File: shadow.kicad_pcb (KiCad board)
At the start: 2 copper layers, 69.8 x 78.7 mm, 95 parts, among them IC2 XB8089D, J1 USB_C_Receptacle, SW1 SW_Push, SW2 SW_Push, SW3 SW_SPST, U1 TCA9548APWR, U2 TCA9548APWR, U3 BQ24092DGQR, U4 TPS61085DGKR, U5 TPS259621DDAT

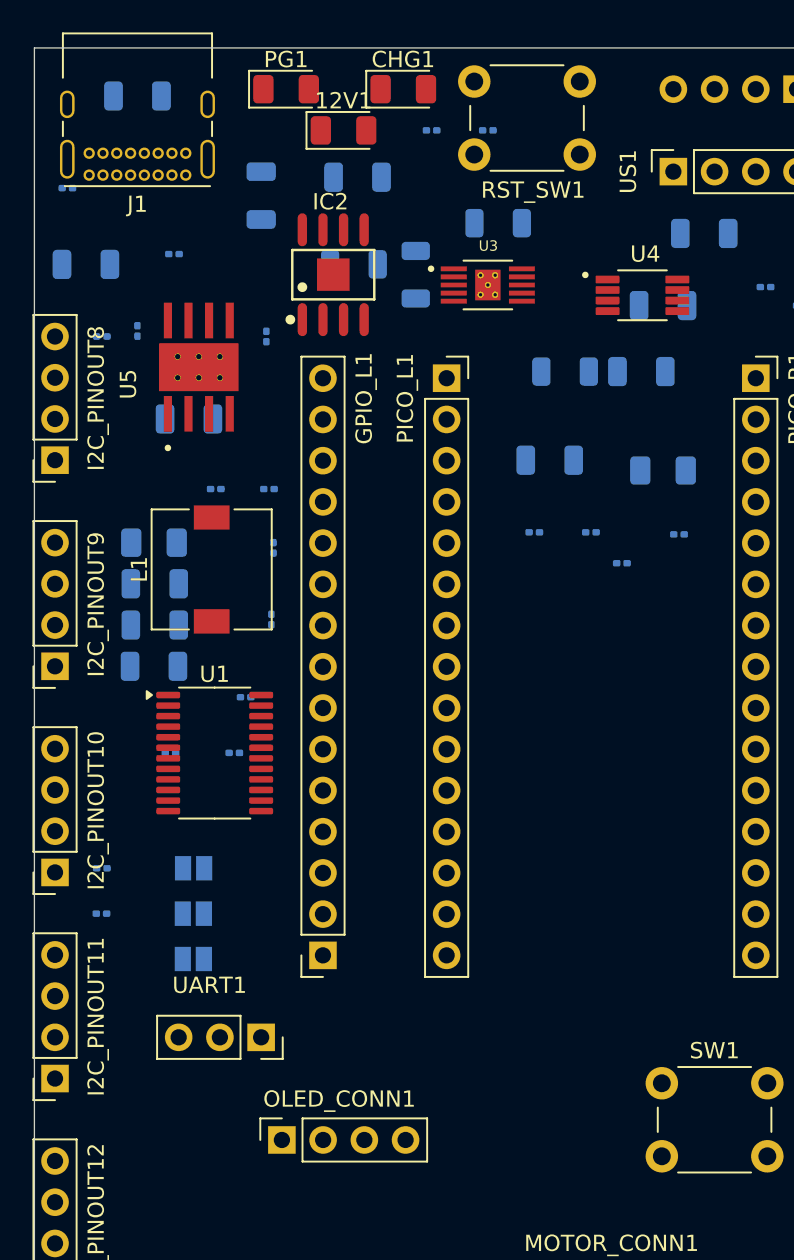
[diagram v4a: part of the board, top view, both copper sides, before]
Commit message: make pcb smaller
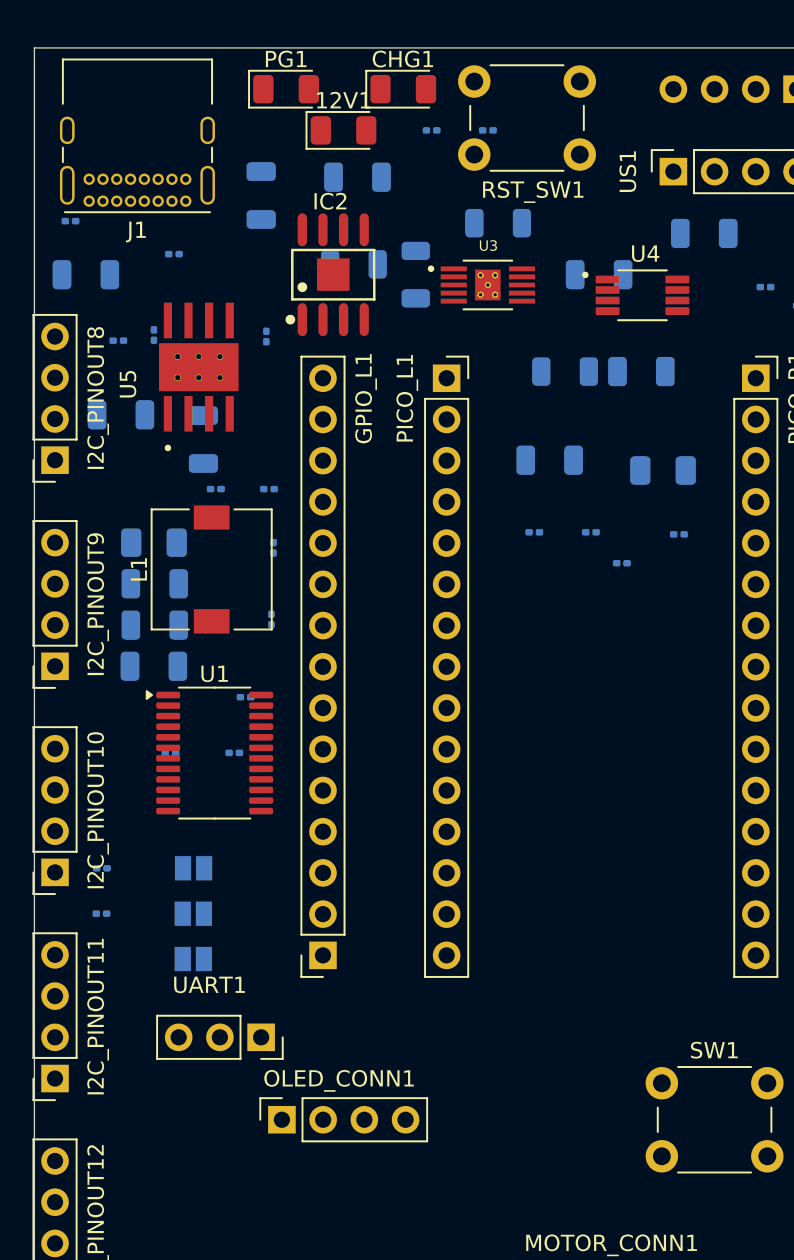
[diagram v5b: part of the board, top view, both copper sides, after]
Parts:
- moved C3 21.6 mm to (95.5, 90.2), turned to -90 degrees
- moved C2 4.37 mm to (119.9, 80.0)
- moved C10 4.20 mm to (90.4, 88.6)
- moved R30 2.04 mm to (87.3, 76.7)
- moved J1 1.61 mm to (94.4, 75.5)
- moved OLED_CONN1 1.24 mm to (100.3, 132.1)
- moved R12 1.05 mm to (92.5, 83.7)
- moved R13 1.05 mm to (90.3, 84.1)
- moved C7 0.64 mm to (88.3, 80.0)
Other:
- board text removed: "OLED TODO: move"
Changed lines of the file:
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@@
 		(tags "connector JST XH vertical")
 		(property "Reference" "BATT_JST1"
-			(at 0.976 4.572 360)
+			(at 0.976 4.572 0)
 			(layer "F.SilkS")
 			(effects
@@
 		)
 		(property "Value" "JST"
-			(at 1.25 4.6 360)
+			(at 1.25 4.6 0)
 			(layer "F.Fab")
 			(effects
@@
 		)
 		(fp_text user "${REFERENCE}"
-			(at 1.25 2.7 360)
+			(at 1.25 2.7 0)
 			(layer "F.Fab")
 			(effects
@@
 		(tags "Through hole socket strip THT 1x03 2.54mm single row")
 		(property "Reference" "UART1"
-			(at -3.2 3.175 360)
+			(at -3.2 3.175 0)
 			(layer "F.SilkS")
 			(effects
@@
 		)
 		(fp_text user "${REFERENCE}"
-			(at 0 2.54 360)
+			(at 0 2.54 0)
 			(layer "F.Fab")
 			(effects
@@
 	(footprint "Connector_PinSocket_2.54mm:PinSocket_1x04_P2.54mm_Vertical"
 		(layer "F.Cu")
-		(at 100.34 133.325 90)
+		(at 100.34 132.08 90)
 		(descr "Through hole straight socket strip, 1x04, 2.54mm pitch, single row (from Kicad 4.0.7), script generated")
 		(tags "Through hole socket strip THT 1x04 2.54mm single row")
@@
 		)
 		(property "Value" "Conn_01x04"
-			(at 0 10.16 90)
+			(at -0.025 3.8 180)
 			(layer "F.Fab")
 			(effects
@@
 		)
 		(fp_text user "${REFERENCE}"
-			(at 0 -2.54 90)
+			(at -3.835 3.8 0)
 			(layer "F.Fab")
 			(effects
@@
 	(footprint "Connector_USB:USB_C_Receptacle_GCT_USB4085"
 		(layer "F.Cu")
-		(at 94.415 73.875 180)
+		(at 94.415 75.48 180)
 		(descr "USB 2.0 Type C Receptacle, https://gct.co/Files/Drawings/USB4085.pdf")
 		(tags "USB Type-C Receptacle Through-hole Right angle")
@@
 		(placed yes)
 		(layer "B.Cu")
-		(at 89.245 83.82 180)
+		(at 90.261 84.074 180)
 		(descr "Resistor SMD 0201 (0603 Metric), square (rectangular) end terminal, IPC_7351 nominal, (Body size source: https://www.vishay.com/docs/20052/crcw0201e3.pdf), generated with kicad-footprint-generator")
 		(tags "resistor")
@@
 		(placed yes)
 		(layer "B.Cu")
-		(at 88.265 79.375 180)
+		(at 88.265 80.01 180)
 		(descr "Capacitor SMD 1206 (3216 Metric), square (rectangular) end terminal, IPC_7351 nominal, (Body size source: IPC-SM-782 page 76, https://www.pcb-3d.com/wordpress/wp-content/uploads/ipc-sm-782a_amendment_1_and_2.pdf), generated with kicad-footprint-generator")
 		(tags "capacitor")
@@
 		(placed yes)
 		(layer "B.Cu")
-		(at 94.615 88.9 180)
+		(at 90.424 88.646 180)
 		(descr "Capacitor SMD 1206 (3216 Metric), square (rectangular) end terminal, IPC_7351 nominal, (Body size source: IPC-SM-782 page 76, https://www.pcb-3d.com/wordpress/wp-content/uploads/ipc-sm-782a_amendment_1_and_2.pdf), generated with kicad-footprint-generator")
 		(tags "capacitor")
@@
 		(placed yes)
 		(layer "B.Cu")
-		(at 123.825 81.915 180)
+		(at 119.888 80.01 180)
 		(descr "Capacitor SMD 1206 (3216 Metric), square (rectangular) end terminal, IPC_7351 nominal, (Body size source: IPC-SM-782 page 76, https://www.pcb-3d.com/wordpress/wp-content/uploads/ipc-sm-782a_amendment_1_and_2.pdf), generated with kicad-footprint-generator")
 		(tags "capacitor")
@@
 		(placed yes)
 		(layer "B.Cu")
-		(at 87.122 74.676)
+		(at 87.31 76.708)
 		(descr "Resistor SMD 0201 (0603 Metric), square (rectangular) end terminal, IPC_7351 nominal, (Body size source: https://www.vishay.com/docs/20052/crcw0201e3.pdf), generated with kicad-footprint-generator")
 		(tags "resistor")
 		(property "Reference" "R30"
-			(at 0 1.05 0)
+			(at 2.195 0 0)
 			(layer "B.SilkS")
 			(effects
@@
 		(tags "capacitor")
 		(property "Reference" "C6"
-			(at 0 1.85 0)
+			(at -0.1925 1.905 0)
 			(layer "B.SilkS")
 			(effects
@@
 		(placed yes)
 		(layer "B.Cu")
-		(at 91.44 69 180)
+		(at 95.504 90.17 -90)
 		(descr "Capacitor SMD 1206 (3216 Metric), square (rectangular) end terminal, IPC_7351 nominal, (Body size source: IPC-SM-782 page 76, https://www.pcb-3d.com/wordpress/wp-content/uploads/ipc-sm-782a_amendment_1_and_2.pdf), generated with kicad-footprint-generator")
 		(tags "capacitor")
 		(property "Reference" "C3"
-			(at 0 1.85 0)
+			(at 0 1.85 90)
 			(layer "B.SilkS")
 			(effects
@@
 		)
 		(property "Value" "10uF"
-			(at 0 -1.85 0)
+			(at 0 -1.85 90)
 			(layer "B.Fab")
 			(effects
@@
 		)
 		(property "Footprint" "Capacitor_SMD:C_1206_3216Metric"
-			(at 0 0 0)
+			(at 0 0 90)
 			(unlocked yes)
 			(layer "B.Fab")
@@
 		)
 		(property "Datasheet" ""
-			(at 0 0 0)
+			(at 0 0 90)
 			(unlocked yes)
 			(layer "B.Fab")
@@
 		)
 		(property "Description" "Unpolarized capacitor"
-			(at 0 0 0)
+			(at 0 0 90)
 			(unlocked yes)
 			(layer "B.Fab")
@@
 		)
 		(fp_line
-			(start 2.3 1.15)
-			(end -2.3 1.15)
+			(start -2.3 1.15)
+			(end -2.3 -1.15)
 			(stroke
 				(width 0.05)
@@
 		)
 		(fp_line
-			(start 2.3 -1.15)
-			(end 2.3 1.15)
+			(start 2.3 1.15)
+			(end -2.3 1.15)
 			(stroke
 				(width 0.05)
@@
 		)
 		(fp_line
-			(start -2.3 1.15)
-			(end -2.3 -1.15)
+			(start -2.3 -1.15)
+			(end 2.3 -1.15)
 			(stroke
 				(width 0.05)
@@
 		)
 		(fp_line
-			(start -2.3 -1.15)
-			(end 2.3 -1.15)
+			(start 2.3 -1.15)
+			(end 2.3 1.15)
 			(stroke
 				(width 0.05)
@@
 		)
 		(fp_line
-			(start 1.6 0.8)
-			(end -1.6 0.8)
+			(start -1.6 0.8)
+			(end -1.6 -0.8)
 			(stroke
 				(width 0.1)
@@
 		)
 		(fp_line
-			(start 1.6 -0.8)
-			(end 1.6 0.8)
+			(start 1.6 0.8)
+			(end -1.6 0.8)
 			(stroke
 				(width 0.1)
@@
 		)
 		(fp_line
-			(start -1.6 0.8)
-			(end -1.6 -0.8)
+			(start -1.6 -0.8)
+			(end 1.6 -0.8)
 			(stroke
 				(width 0.1)
@@
 		)
 		(fp_line
-			(start -1.6 -0.8)
-			(end 1.6 -0.8)
+			(start 1.6 -0.8)
+			(end 1.6 0.8)
 			(stroke
 				(width 0.1)
@@
 		)
 		(fp_text user "${REFERENCE}"
-			(at 0 0 0)
+			(at 0 0 90)
 			(layer "B.Fab")
 			(effects
@@
 		)
 		(pad "1" smd roundrect
-			(at -1.475 0 180)
+			(at -1.475 0 270)
 			(size 1.15 1.8)
 			(layers "B.Cu" "B.Paste" "B.Mask")
@@
 		)
 		(pad "2" smd roundrect
-			(at 1.475 0 180)
+			(at 1.475 0 270)
 			(size 1.15 1.8)
 			(layers "B.Cu" "B.Paste" "B.Mask")
@@
 		(placed yes)
 		(layer "B.Cu")
-		(at 91.44 83.475 90)
+		(at 92.456 83.729 90)
 		(descr "Resistor SMD 0201 (0603 Metric), square (rectangular) end terminal, IPC_7351 nominal, (Body size source: https://www.vishay.com/docs/20052/crcw0201e3.pdf), generated with kicad-footprint-generator")
 		(tags "resistor")
@@
 		)
 	)
-	(gr_text "OLED\nTODO: move"
-		(at 101.6 139.7 0)
-		(layer "User.2")
-		(effects
-			(font
-				(size 1 1)
-				(thickness 0.15)
-			)
-			(justify left bottom)
-		)
-	)

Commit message: more work on pcb
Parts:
- moved C14 0.38 mm to (98.1, 106.4)
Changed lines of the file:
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@@
 		)
 		(property "Value" "TCA9548APWR"
-			(at 24.155 3.27 0)
+			(at -1.2015 1.513 0)
 			(layer "B.Fab")
 			(effects
@@
 		(at 95.22 85.71 90)
 		(property "Reference" "U5"
-			(at -1.05 -4.335 90)
+			(at 4.938 -0.224 180)
 			(layer "F.SilkS")
 			(effects
@@
 		(tags "LED")
 		(property "Reference" "12V1"
-			(at 0 -1.82 0)
+			(at 0 2.032 0)
 			(layer "F.SilkS")
 			(effects
@@
 		(tags "resistor")
 		(property "Reference" "R33"
-			(at 0 1.05 90)
+			(at 2.123 -0.127 90)
 			(layer "B.SilkS")
 			(effects
@@
 		(placed yes)
 		(layer "B.Cu")
-		(at 98.105 106.045 180)
+		(at 98.105 106.426 180)
 		(descr "Capacitor SMD 0201 (0603 Metric), square (rectangular) end terminal, IPC_7351 nominal, (Body size source: https://www.vishay.com/docs/20052/crcw0201e3.pdf), generated with kicad-footprint-generator")
 		(tags "capacitor")
 		(property "Reference" "C14"
-			(at 0.091 -1.016 0)
+			(at 2.347 -0.127 0)
 			(layer "B.SilkS")
 			(effects

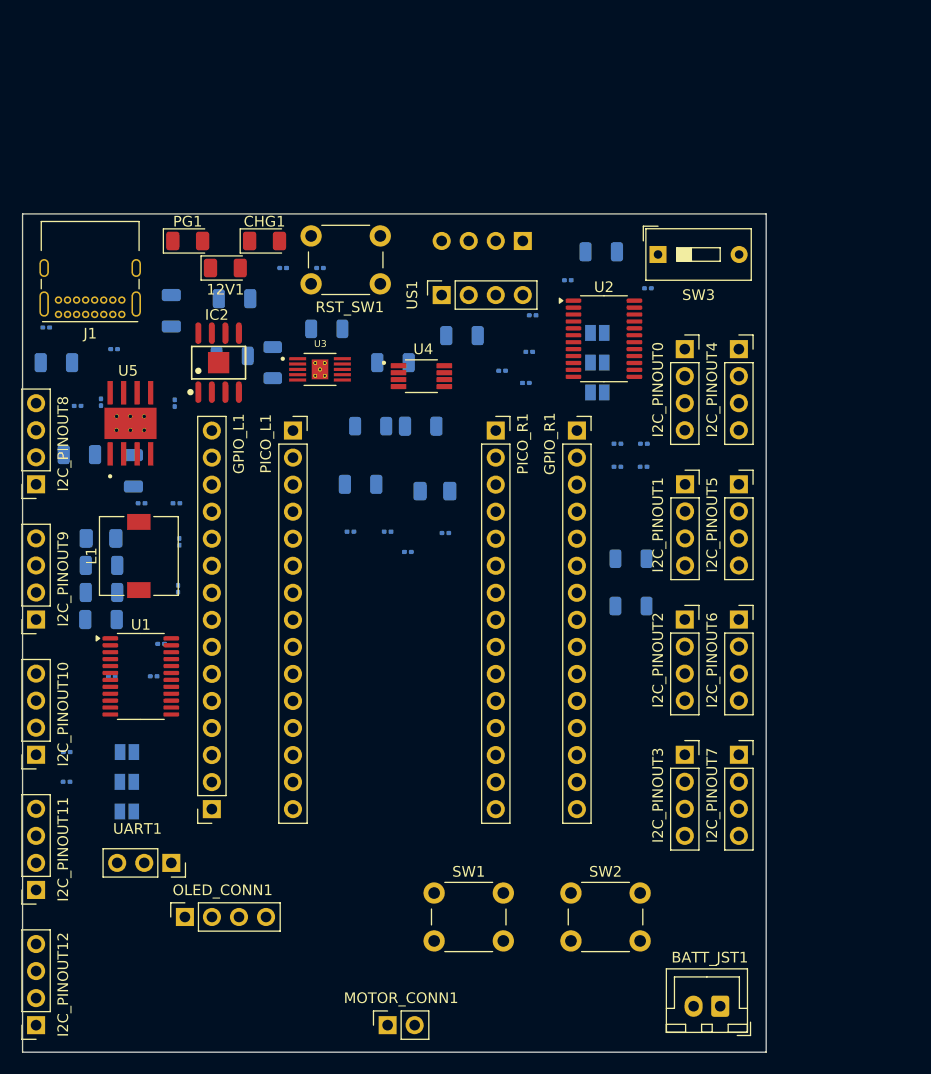
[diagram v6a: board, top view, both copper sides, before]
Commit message: add mounting holes
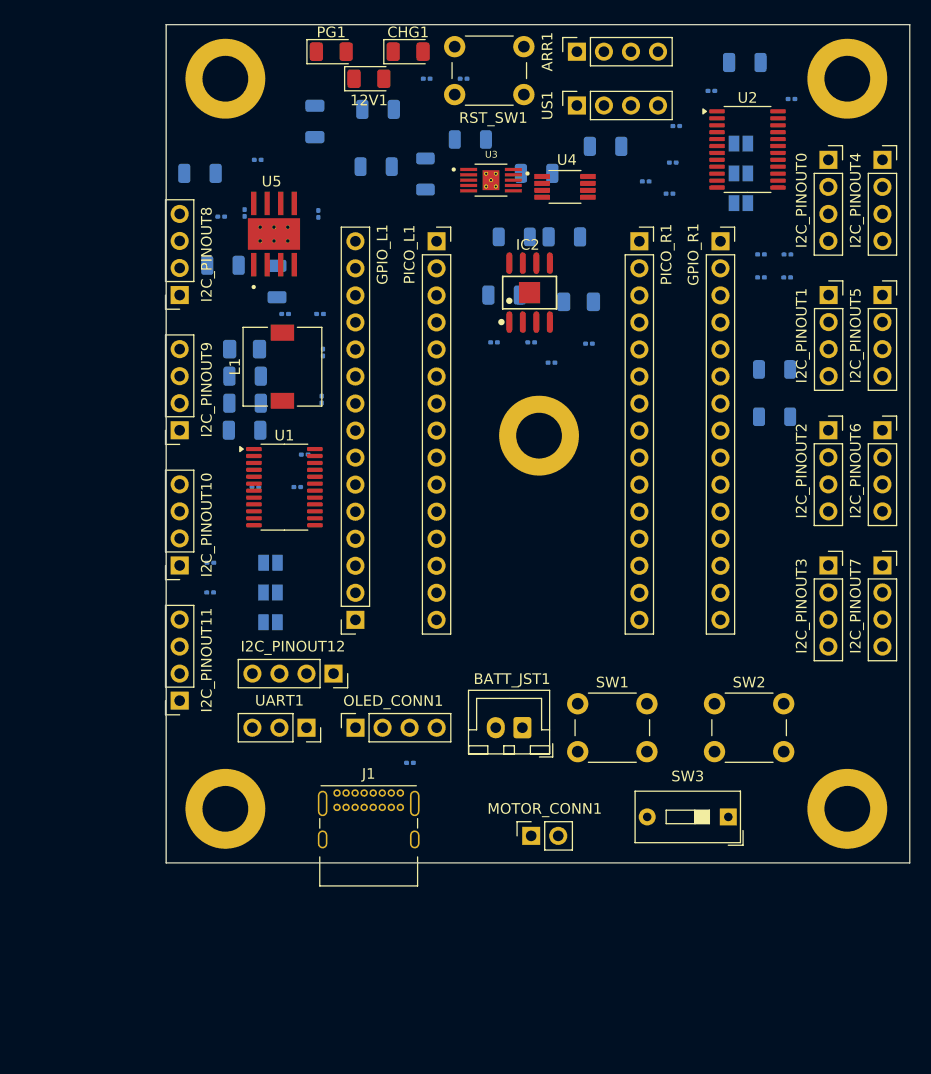
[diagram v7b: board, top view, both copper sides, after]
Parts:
- added REF**: MountingHole_4.3mm_M4_DIN965_Pad, MountingHole:MountingHole_4.3mm_M4_DIN965_Pad, F.Cu at (104.1, 53.3)
- added REF**: MountingHole_4.3mm_M4_DIN965_Pad, MountingHole:MountingHole_4.3mm_M4_DIN965_Pad, F.Cu at (104.1, 121.9)
- added REF**: MountingHole_4.3mm_M4_DIN965_Pad, MountingHole:MountingHole_4.3mm_M4_DIN965_Pad, F.Cu at (162.6, 121.9)
- added REF**: MountingHole_4.3mm_M4_DIN965_Pad, MountingHole:MountingHole_4.3mm_M4_DIN965_Pad, F.Cu at (133.6, 86.9)
- added REF**: MountingHole_4.3mm_M4_DIN965_Pad, MountingHole:MountingHole_4.3mm_M4_DIN965_Pad, F.Cu at (162.6, 53.3)
- ARR1: moved to F.Cu
- moved R30 53.3 mm to (121.5, 117.6), turned to 180 degrees
- moved SW3 53.2 mm to (151.4, 122.7), turned to 180 degrees
- moved J1 49.3 mm to (114.6, 120.4), turned to 0 degrees
- moved I2C_PINOUT12 43.3 mm to (114.3, 109.2), turned to -90 degrees
- moved BATT_JST1 32.1 mm to (132.0, 114.3)
- moved IC2 29.9 mm to (132.7, 73.4)
- moved U3 24.0 mm to (129.1, 62.9)
- moved OLED_CONN1 23.9 mm to (116.4, 114.3)
- moved R7 22.8 mm to (122.9, 62.3)
- moved R5 22.3 mm to (118.3, 61.6)
- moved R26 22.3 mm to (149.8, 54.5)
- moved I2C_PINOUT2 22.3 mm to (160.8, 86.4)
- moved I2C_PINOUT3 22.3 mm to (160.8, 99.1)
- moved U2 22.3 mm to (153.2, 60.0)
- moved I2C_PINOUT0 22.3 mm to (160.8, 61.0)
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
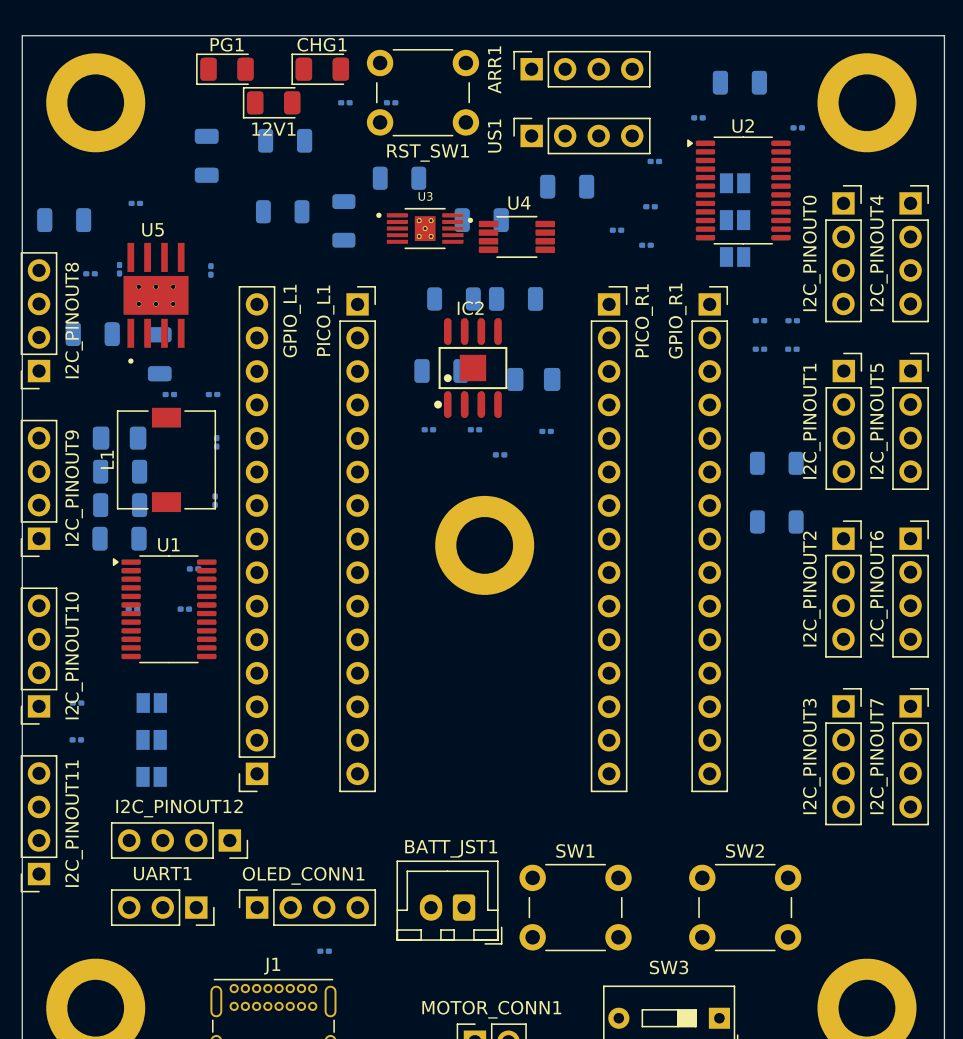
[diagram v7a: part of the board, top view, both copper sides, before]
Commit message: ground mounting holes
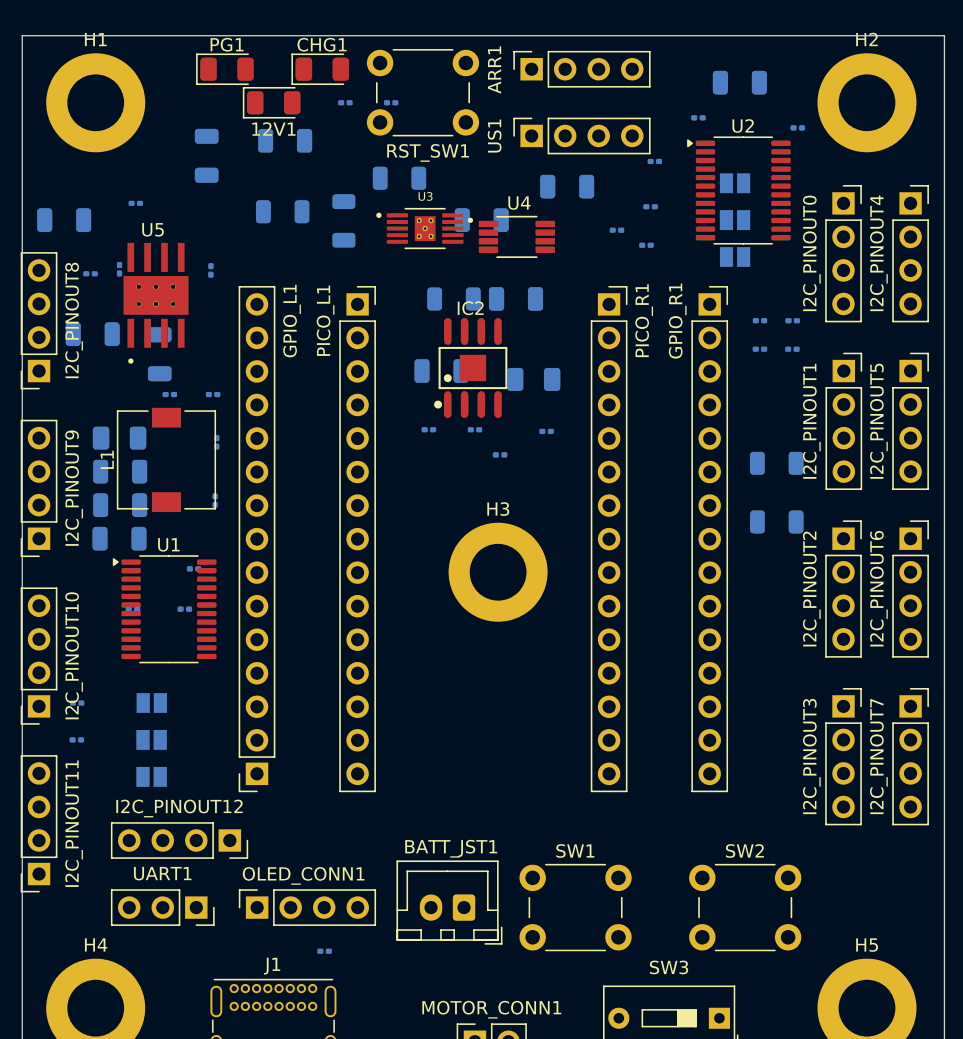
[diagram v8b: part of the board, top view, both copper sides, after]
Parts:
- removed REF** (x5): MountingHole_4.3mm_M4_DIN965_Pad, MountingHole:MountingHole_4.3mm_M4_DIN965_Pad
- added H1: MountingHole_Pad, MountingHole:MountingHole_4.3mm_M4_DIN965_Pad, F.Cu at (104.1, 53.3)
- added H2: MountingHole_Pad, MountingHole:MountingHole_4.3mm_M4_DIN965_Pad, F.Cu at (162.6, 53.3)
- added H3: MountingHole_Pad, MountingHole:MountingHole_4.3mm_M4_DIN965_Pad, F.Cu at (134.6, 88.9)
- added H4: MountingHole_Pad, MountingHole:MountingHole_4.3mm_M4_DIN965_Pad, F.Cu at (104.1, 121.9)
- added H5: MountingHole_Pad, MountingHole:MountingHole_4.3mm_M4_DIN965_Pad, F.Cu at (162.6, 121.9)
